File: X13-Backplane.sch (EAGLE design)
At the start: 36 parts, among them J1 PXC-PTSM-04-RA-1778641, J2 PXC-PTSM-04-RA-1778641, J3 PXC-8-RA-1778683, J4 PXC-PTSM-04-RA-1778641, J5 PXC-PTSM-04-RA-1778641, J8 PXC-8-RA-1778683

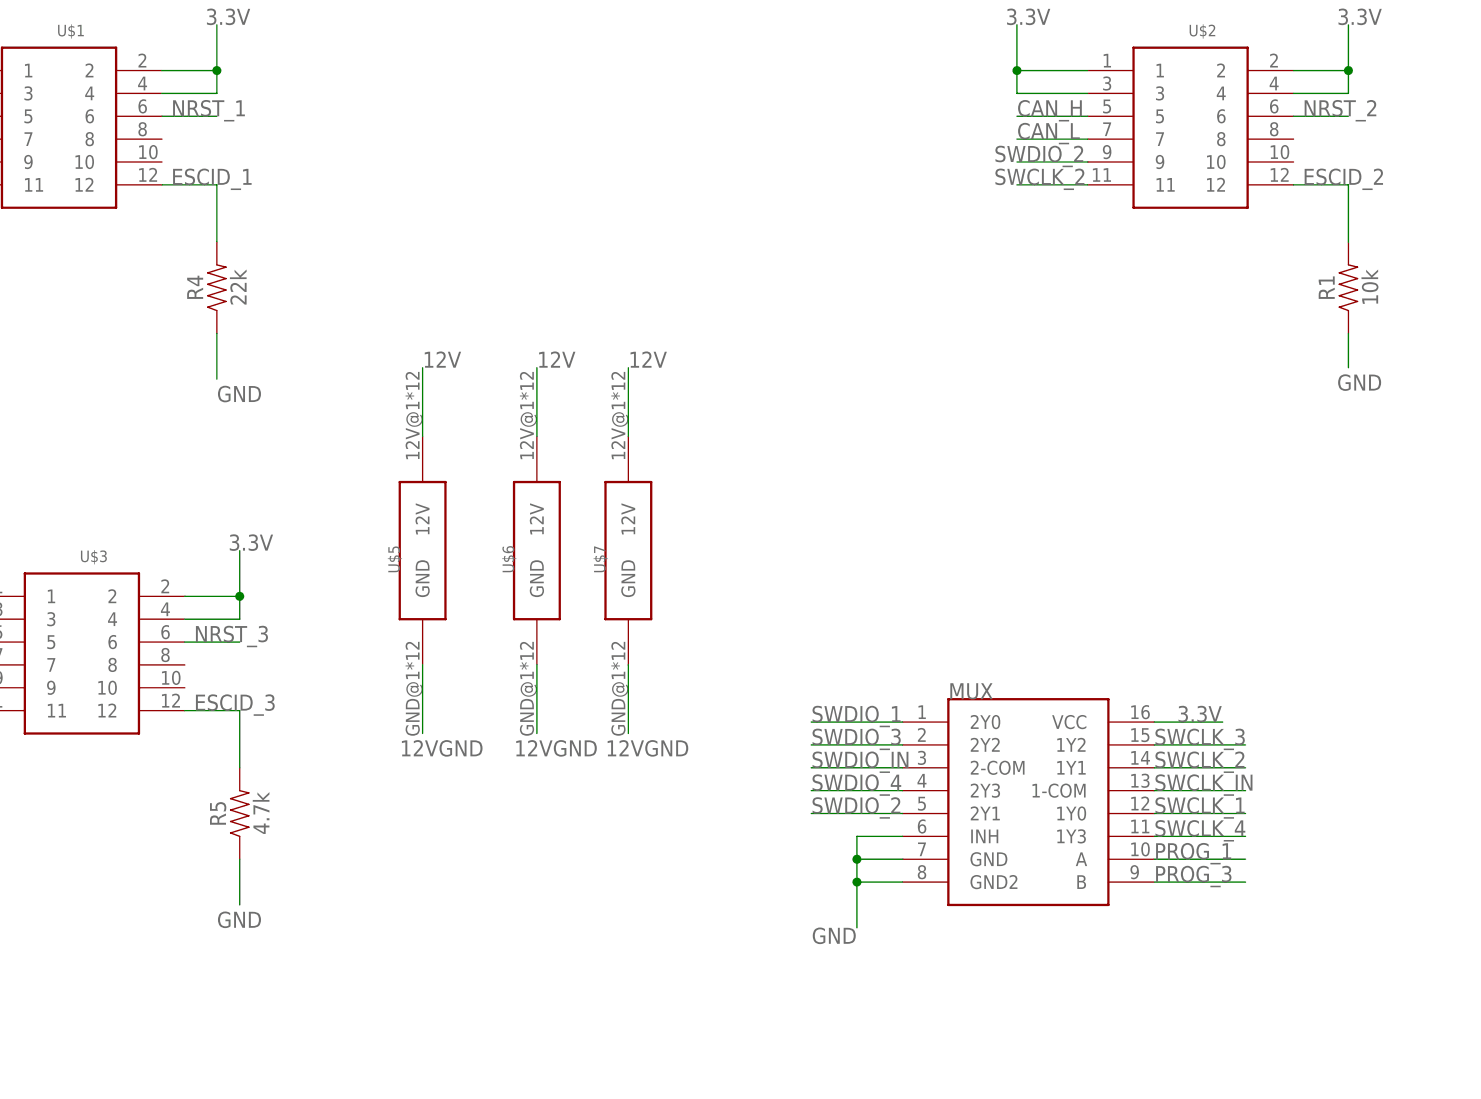
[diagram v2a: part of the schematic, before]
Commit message: OPE. GND connections were missing on esc controller connector
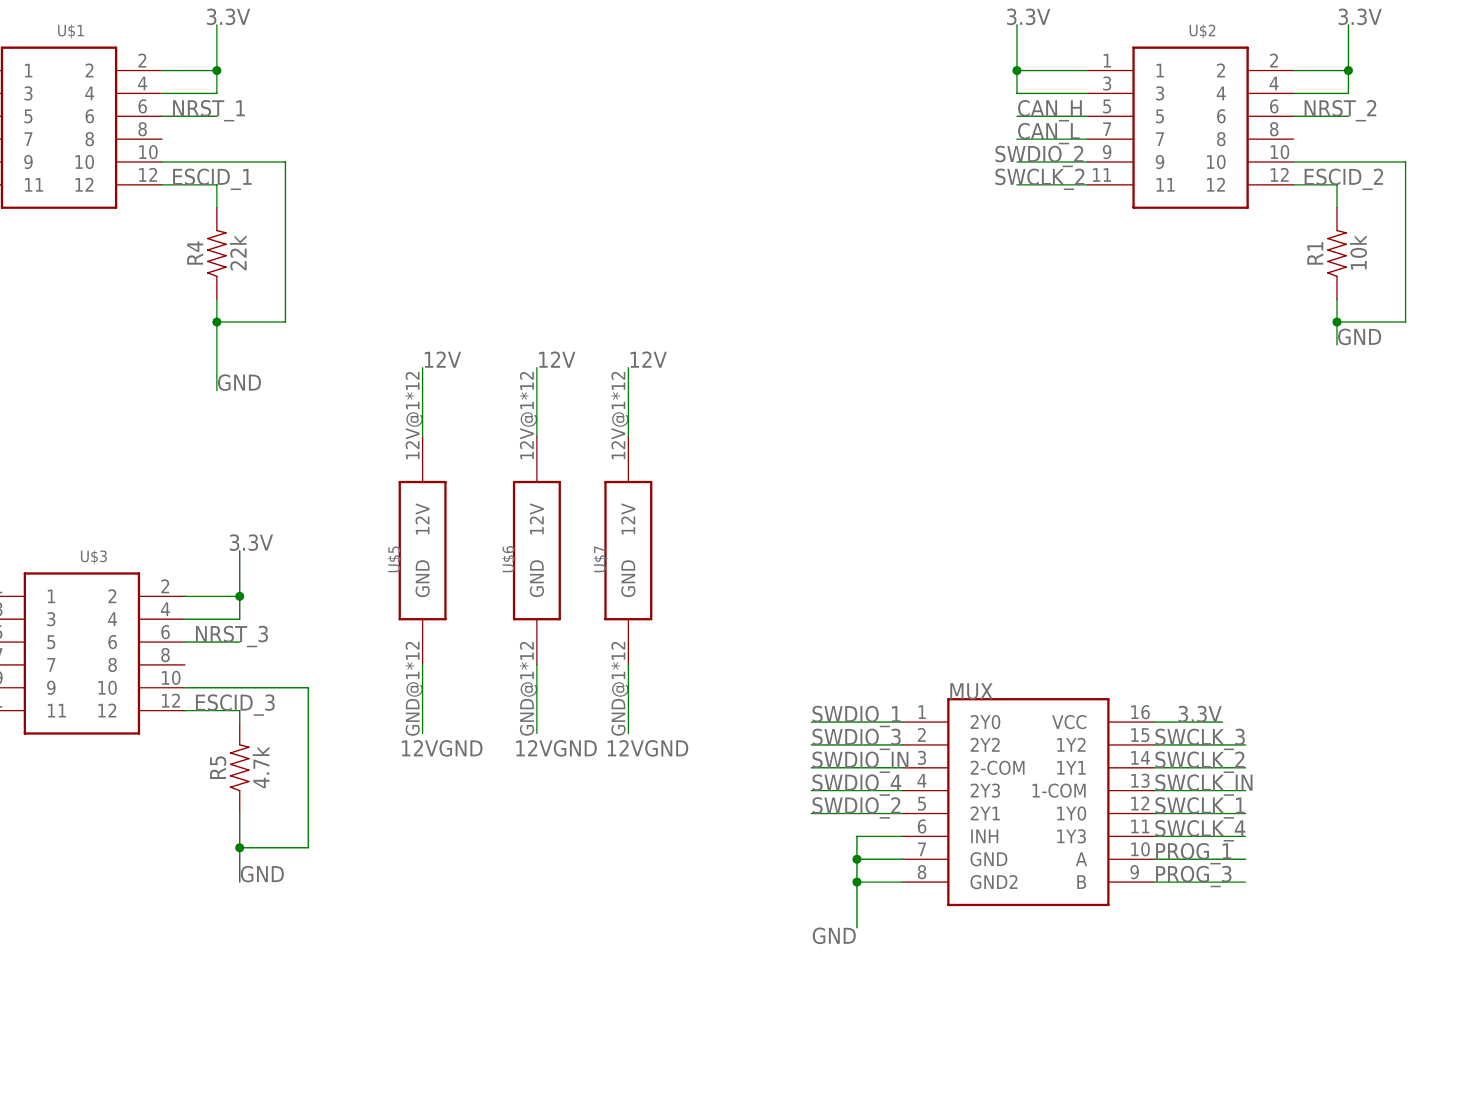
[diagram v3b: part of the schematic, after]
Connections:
- net GND: now also U$1.10, U$2.10, U$3.10
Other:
- moved on the sheet: R1, R4, R5
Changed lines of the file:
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@@
 <attribute name="VALUE" x="191.77" y="-109.22" size="1.778" layer="96" rot="R180"/>
 </instance>
-<instance part="R4" gate="G$1" x="124.46" y="123.19" smashed="yes" rot="R90">
-<attribute name="NAME" x="122.936" y="123.19" size="1.778" layer="95" font="vector" rot="R90" align="bottom-center"/>
-<attribute name="VALUE" x="125.984" y="123.19" size="1.778" layer="96" font="vector" rot="R90" align="top-center"/>
-</instance>
-<instance part="R1" gate="G$1" x="250.19" y="123.19" smashed="yes" rot="R90">
-<attribute name="NAME" x="248.666" y="123.19" size="1.778" layer="95" font="vector" rot="R90" align="bottom-center"/>
-<attribute name="VALUE" x="251.714" y="123.19" size="1.778" layer="96" font="vector" rot="R90" align="top-center"/>
-</instance>
-<instance part="R5" gate="G$1" x="127" y="64.77" smashed="yes" rot="R90">
-<attribute name="NAME" x="125.476" y="64.77" size="1.778" layer="95" font="vector" rot="R90" align="bottom-center"/>
-<attribute name="VALUE" x="128.524" y="64.77" size="1.778" layer="96" font="vector" rot="R90" align="top-center"/>
+<instance part="R4" gate="G$1" x="124.46" y="127" smashed="yes" rot="R90">
+<attribute name="NAME" x="122.936" y="127" size="1.778" layer="95" font="vector" rot="R90" align="bottom-center"/>
+<attribute name="VALUE" x="125.984" y="127" size="1.778" layer="96" font="vector" rot="R90" align="top-center"/>
+</instance>
+<instance part="R1" gate="G$1" x="248.92" y="127" smashed="yes" rot="R90">
+<attribute name="NAME" x="247.396" y="127" size="1.778" layer="95" font="vector" rot="R90" align="bottom-center"/>
+<attribute name="VALUE" x="250.444" y="127" size="1.778" layer="96" font="vector" rot="R90" align="top-center"/>
+</instance>
+<instance part="R5" gate="G$1" x="127" y="69.85" smashed="yes" rot="R90">
+<attribute name="NAME" x="125.476" y="69.85" size="1.778" layer="95" font="vector" rot="R90" align="bottom-center"/>
+<attribute name="VALUE" x="128.524" y="69.85" size="1.778" layer="96" font="vector" rot="R90" align="top-center"/>
 </instance>
 <instance part="DIST_TO_BACKPLANE" gate="G$1" x="26.67" y="-40.64" smashed="yes">
@@
 <segment>
 <pinref part="R4" gate="G$1" pin="1"/>
-<wire x1="124.46" y1="118.11" x2="124.46" y2="113.03" width="0.1524" layer="91"/>
-<label x="124.46" y="110.49" size="1.778" layer="95"/>
+<wire x1="124.46" y1="121.92" x2="124.46" y2="119.38" width="0.1524" layer="91"/>
+<label x="124.46" y="111.76" size="1.778" layer="95"/>
+<pinref part="U$1" gate="G$1" pin="10"/>
+<wire x1="124.46" y1="119.38" x2="124.46" y2="111.76" width="0.1524" layer="91"/>
+<wire x1="118.364" y1="137.16" x2="132.08" y2="137.16" width="0.1524" layer="91"/>
+<wire x1="132.08" y1="137.16" x2="132.08" y2="119.38" width="0.1524" layer="91"/>
+<wire x1="132.08" y1="119.38" x2="124.46" y2="119.38" width="0.1524" layer="91"/>
+<junction x="124.46" y="119.38"/>
 </segment>
 <segment>
 <pinref part="R1" gate="G$1" pin="1"/>
-<wire x1="250.19" y1="118.11" x2="250.19" y2="114.3" width="0.1524" layer="91"/>
-<label x="248.92" y="111.76" size="1.778" layer="95"/>
+<wire x1="248.92" y1="121.92" x2="248.92" y2="119.38" width="0.1524" layer="91"/>
+<label x="248.92" y="116.84" size="1.778" layer="95"/>
+<pinref part="U$2" gate="G$1" pin="10"/>
+<wire x1="248.92" y1="119.38" x2="248.92" y2="116.84" width="0.1524" layer="91"/>
+<wire x1="244.094" y1="137.16" x2="256.54" y2="137.16" width="0.1524" layer="91"/>
+<wire x1="256.54" y1="137.16" x2="256.54" y2="119.38" width="0.1524" layer="91"/>
+<wire x1="256.54" y1="119.38" x2="248.92" y2="119.38" width="0.1524" layer="91"/>
+<junction x="248.92" y="119.38"/>
 </segment>
 <segment>
 <pinref part="R5" gate="G$1" pin="1"/>
-<wire x1="127" y1="59.69" x2="127" y2="54.61" width="0.1524" layer="91"/>
-<label x="124.46" y="52.07" size="1.778" layer="95"/>
+<wire x1="127" y1="64.77" x2="127" y2="60.96" width="0.1524" layer="91"/>
+<label x="127" y="57.15" size="1.778" layer="95"/>
+<pinref part="U$3" gate="G$1" pin="10"/>
+<wire x1="127" y1="60.96" x2="127" y2="57.15" width="0.1524" layer="91"/>
+<wire x1="120.904" y1="78.74" x2="134.62" y2="78.74" width="0.1524" layer="91"/>
+<wire x1="134.62" y1="78.74" x2="134.62" y2="60.96" width="0.1524" layer="91"/>
+<wire x1="127" y1="60.96" x2="134.62" y2="60.96" width="0.1524" layer="91"/>
+<junction x="127" y="60.96"/>
 </segment>
 <segment>
@@
 <pinref part="R4" gate="G$1" pin="2"/>
 <wire x1="118.364" y1="134.62" x2="124.46" y2="134.62" width="0.1524" layer="91"/>
-<wire x1="124.46" y1="134.62" x2="124.46" y2="128.27" width="0.1524" layer="91"/>
+<wire x1="124.46" y1="134.62" x2="124.46" y2="132.08" width="0.1524" layer="91"/>
 <label x="119.38" y="134.62" size="1.778" layer="95"/>
 <pinref part="U$1" gate="G$1" pin="12"/>
@@
 <net name="ESCID_2" class="0">
 <segment>
-<wire x1="244.094" y1="134.62" x2="250.19" y2="134.62" width="0.1524" layer="91"/>
-<wire x1="250.19" y1="134.62" x2="250.19" y2="128.27" width="0.1524" layer="91"/>
+<wire x1="244.094" y1="134.62" x2="248.92" y2="134.62" width="0.1524" layer="91"/>
+<wire x1="248.92" y1="134.62" x2="248.92" y2="132.08" width="0.1524" layer="91"/>
 <label x="245.11" y="134.62" size="1.778" layer="95"/>
 <pinref part="R1" gate="G$1" pin="2"/>
@@
 <segment>
 <wire x1="120.904" y1="76.2" x2="127" y2="76.2" width="0.1524" layer="91"/>
-<wire x1="127" y1="76.2" x2="127" y2="69.85" width="0.1524" layer="91"/>
+<wire x1="127" y1="76.2" x2="127" y2="74.93" width="0.1524" layer="91"/>
 <label x="121.92" y="76.2" size="1.778" layer="95"/>
 <pinref part="R5" gate="G$1" pin="2"/>

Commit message: moved 2x6 logic dist block in and add conn for switch as backup
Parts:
- added J7: POE_TERMINAL, Dist_POE:POE_TERMINAL
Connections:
- net 5V: now also J7.1
- net GND: now also J7.2
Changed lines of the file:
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@@
 <part name="D4" library="SparkFun-DiscreteSemi" library_urn="urn:adsk.eagle:library:514" deviceset="DIODE-SCHOTTKY" device="-PMEG4005EJ" package3d_urn="urn:adsk.eagle:package:38441/1" value="0.5A/40V/420mV"/>
 <part name="C5" library="Panasonic 47 uF cap - EEE-1CA470SP" deviceset="47UF-POLAR" device="-PANASONIC_D-35V-20%" package3d_urn="urn:adsk.eagle:package:24384400/2" value="47uF"/>
+<part name="J7" library="Dist_POE" deviceset="POE_TERMINAL" device="" package3d_urn="urn:adsk.eagle:package:25763292/2"/>
 </parts>
 <sheets>
@@
 <attribute name="VALUE" x="141.986" y="-58.801" size="1.778" layer="96" font="vector"/>
 </instance>
+<instance part="J7" gate="A" x="236.22" y="-88.9" smashed="yes">
+<attribute name="NAME" x="231.4956" y="-82.3214" size="2.0828" layer="95" ratio="6" rot="SR0"/>
+</instance>
 </instances>
 <busses>
@@
 <label x="138.43" y="-71.12" size="1.778" layer="95"/>
 </segment>
+<segment>
+<pinref part="J7" gate="A" pin="2"/>
+<wire x1="227.33" y1="-90.17" x2="226.06" y2="-90.17" width="0.1524" layer="91"/>
+<wire x1="226.06" y1="-90.17" x2="226.06" y2="-93.98" width="0.1524" layer="91"/>
+<label x="226.06" y="-93.98" size="1.778" layer="95"/>
+</segment>
 </net>
 <net name="SWDIO_3" class="0">
@@
 <label x="242.57" y="-113.03" size="1.778" layer="95"/>
 </segment>
-</net>
+<segment>
+<pinref part="J7" gate="A" pin="1"/>
+<wire x1="227.33" y1="-87.63" x2="226.06" y2="-87.63" width="0.1524" layer="91"/>
+<wire x1="226.06" y1="-87.63" x2="226.06" y2="-83.82" width="0.1524" layer="91"/>
+<label x="226.06" y="-83.82" size="1.778" layer="95"/>
+</segment>
+</net>

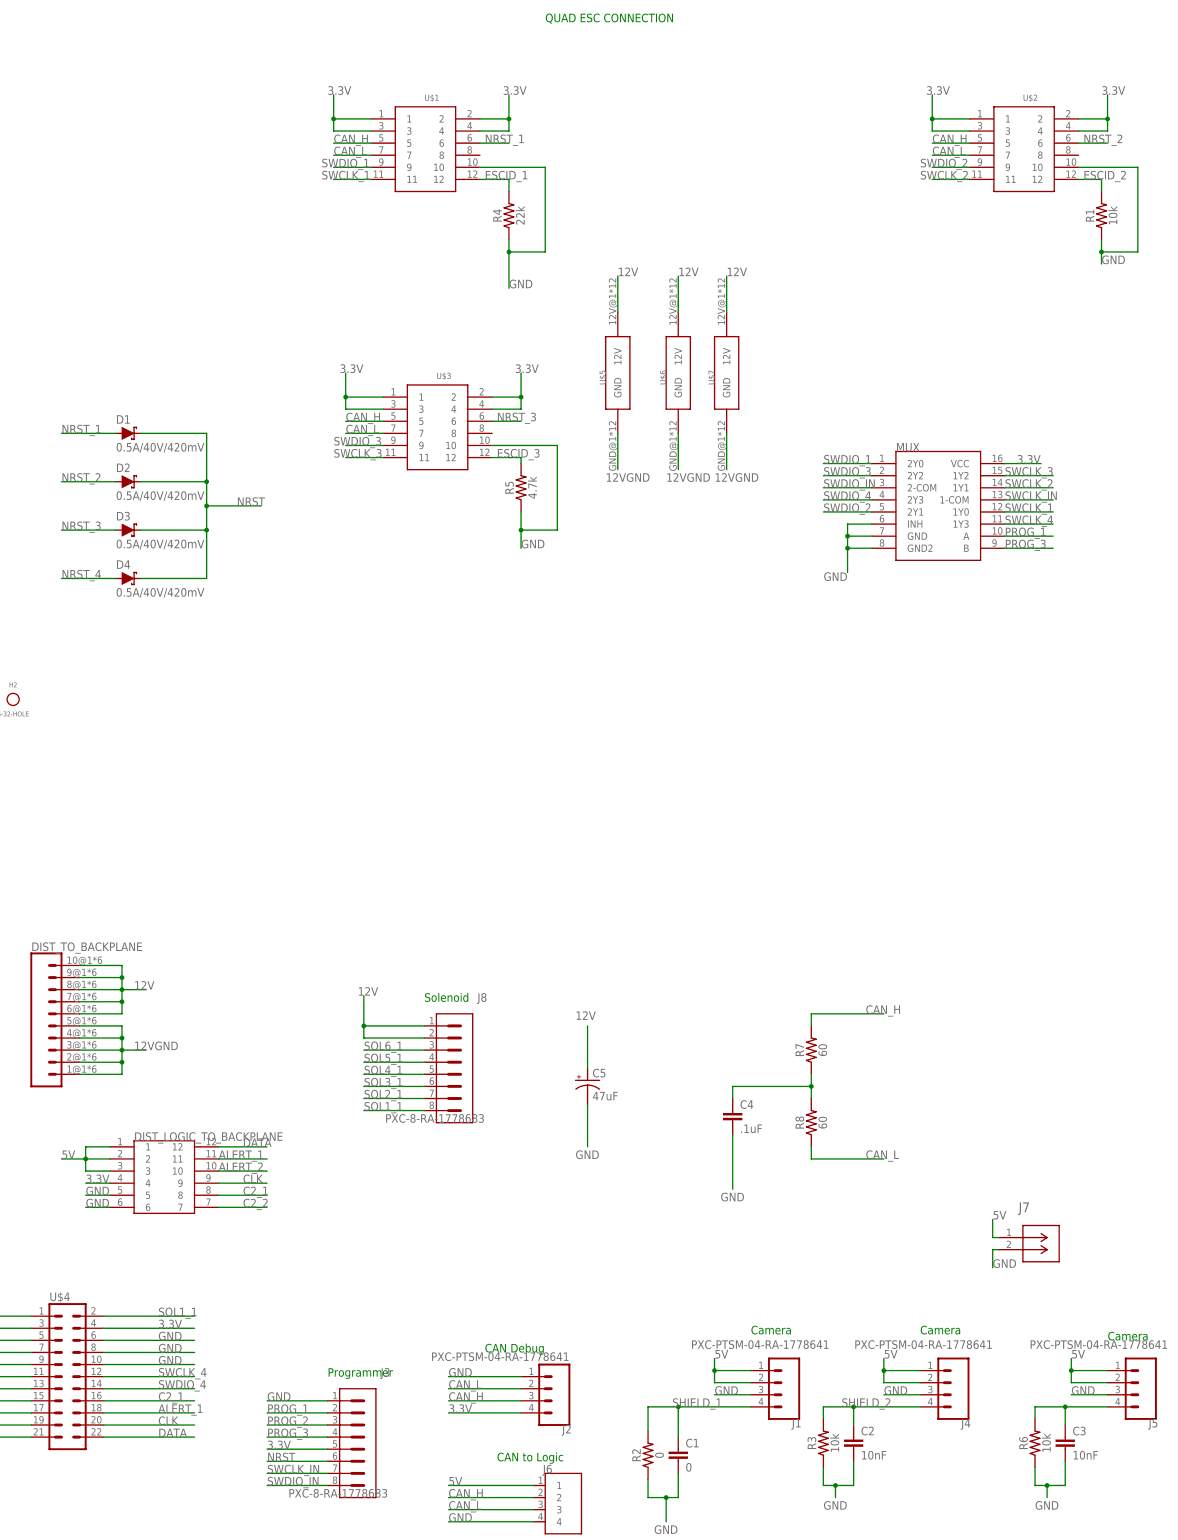
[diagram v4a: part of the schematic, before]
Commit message: Add reset switch for all micros, move connectors in
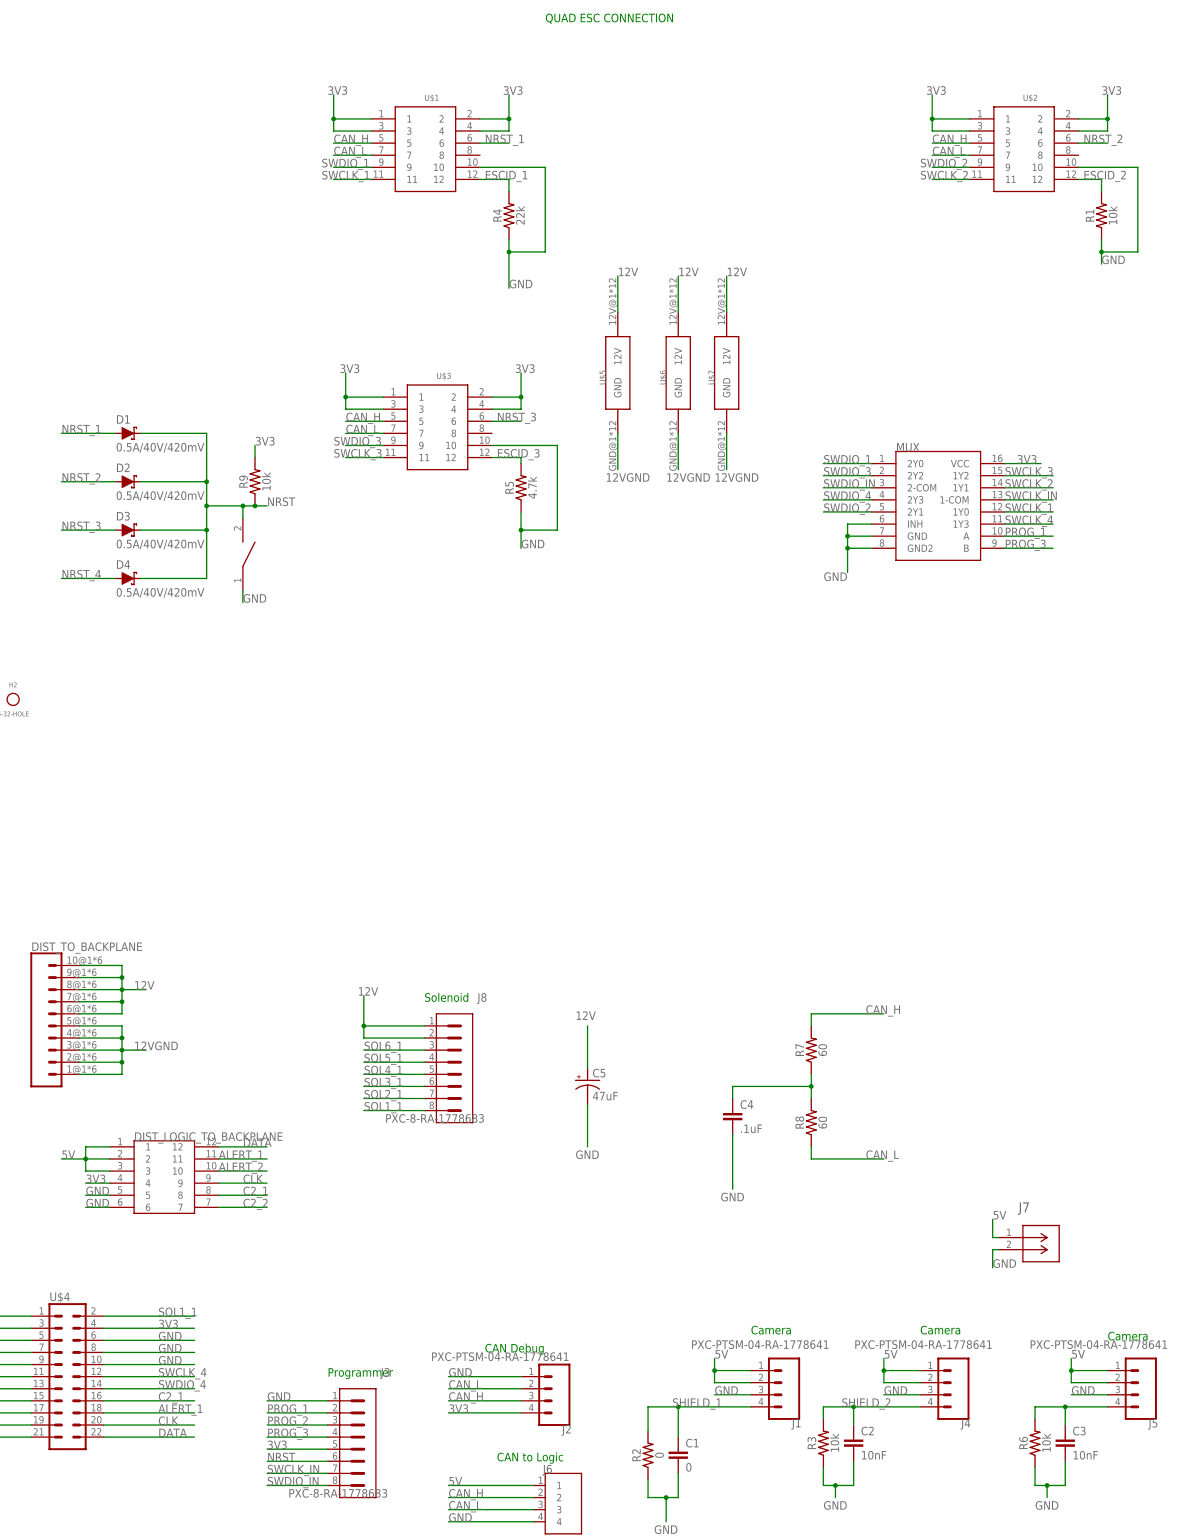
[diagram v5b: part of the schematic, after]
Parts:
- added R9: 10k, SparkFun-Resistors:10KOHM-0603-1/10W-1%
- added U$8: (no value), OTHER, Push button - FSM2JMTR:DISCRETECOMPONENTS_SWITCH
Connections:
- removed net 3.3V: DIST_LOGIC_TO_BACKPLANE.4, J2.4, J3.5, MUX.VCC, U$1.1, U$1.2, U$1.3, U$1.4, U$2.1, U$2.2, U$2.3, U$2.4, U$3.1, U$3.2, U$3.3, U$3.4, U$4.4
- new net 3V3: DIST_LOGIC_TO_BACKPLANE.4, J2.4, J3.5, MUX.VCC, R9.2, U$1.1, U$1.2, U$1.3, U$1.4, U$2.1, U$2.2, U$2.3, U$2.4, U$3.1, U$3.2, U$3.3, U$3.4, U$4.4
- net GND: now also U$8.P$1
- net NRST: now also R9.1, U$8.P$2
